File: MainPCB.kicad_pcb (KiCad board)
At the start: 2 copper layers, 1.7 x 9.8 mm, 78 parts, among them IC1 VNH7070ASTR, IC2 VNH7070ASTR, IC3 VNH7070ASTR, IC4 VNH7070ASTR, IC5 VNH7070ASTR, J1 Conn_01x06, J10 Conn_01x02, J11 Conn_01x03, J13 Conn_01x03, J14 Conn_01x02, J2 RaspberryPi, J4 Conn_01x02, J5 Screw_Terminal_01x02, J6 Conn_02x05_Odd_Even, J8 Conn_01x02, J9 Conn_01x02, M1 Motor_DC, M2 Motor_DC, M3 Motor_DC, M4 Motor_DC, M5 Motor_DC, SW1 SW_DPST_x2, SW2 SW_SPDT, SW3 SW_SPDT, SW4 SW_SPDT, SW5 SW_SPDT, SW6 SW_DPST_x2, U1 V_Regulator3.3v, U10 N channel, U12 Teensy4.1, U2 V_Regulator5v, U6 N channel

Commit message: Placement Done
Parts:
- removed C15: 0.1uf, Capacitor_SMD:C_0805_2012Metric_Pad1.18x1.45mm_HandSolder
- removed IC5: VNH7070ASTR, VNH:SOIC127P600X175-16N
- removed J13: Conn_01x03, Connector_PinHeader_2.54mm:PinHeader_1x03_P2.54mm_Vertical
- removed J14: Conn_01x02, Connector_JST:JST_XH_B2B-XH-A_1x02_P2.50mm_Vertical
- removed M5: Motor_DC, Connector_JST:JST_XH_B2B-XH-AM_1x02_P2.50mm_Vertical
- removed R19: 0, Resistor_SMD:R_0805_2012Metric_Pad1.20x1.40mm_HandSolder
- removed R20: 1, Resistor_SMD:R_0805_2012Metric_Pad1.20x1.40mm_HandSolder
- removed R23, R24, R25: 100, Resistor_SMD:R_0805_2012Metric_Pad1.20x1.40mm_HandSolder
- added J12: Conn_01x03, Connector_JST:JST_XH_B3B-XH-A_1x03_P2.50mm_Vertical, F.Cu at (143.5, 82.0)
- added J3: Conn_01x12, Connector_IDC:IDC-Header_2x06_P2.54mm_Vertical, B.Cu at (149.9, 92.9)
- added J7: Conn_01x02, Connector_JST:JST_XH_B2B-XH-A_1x02_P2.50mm_Vertical, F.Cu at (91.7, 69.3)
- added JP1: SolderJumper_2_Open, Jumper:SolderJumper-2_P1.3mm_Open_RoundedPad1.0x1.5mm, F.Cu at (91.5, 97.0)
- added JP2: SolderJumper_2_Open, Jumper:SolderJumper-2_P1.3mm_Open_RoundedPad1.0x1.5mm, F.Cu at (91.5, 100.5)
- added MOD1: RCJ-COM-2024, RCJ-COM-MOD:RCJ-COM-2024, F.Cu at (133.6, 147.8)
- added U3: BoostConverter, BoostConverter:Boost_Convertor_LM2577, F.Cu at (76.4, 141.2)
- added U4: BNO055, BNO055:BNO055, F.Cu at (119.0, 90.0)
- C11, C12, C13, C14, C3, C4, C5, C6, C7, C8, IC1, IC2, IC3, IC4, R1, R10, R11, R12, R13, R14, R15, R16, R17, R18, R2, R3, R4, R5, R6, R7, R9: moved to B.Cu
- J10, J8, J9: footprint Connector_PinHeader_2.54mm:PinHeader_1x02_P2.54mm_Vertical -> Connector_JST:JST_XH_B2B-XH-A_1x02_P2.50mm_Vertical
- J11: footprint Connector_PinHeader_2.54mm:PinHeader_1x03_P2.54mm_Vertical -> Connector_JST:JST_XH_B3B-XH-A_1x03_P2.50mm_Vertical; moved to B.Cu
- J6: value Conn_02x05_Odd_Even -> Conn_01x03; footprint Connector_IDC:IDC-Header_2x05_P2.54mm_Vertical -> Connector_JST:JST_XH_B3B-XH-A_1x03_P2.50mm_Vertical
- M1, M2, M3, M4: footprint Connector_JST:JST_XH_B2B-XH-AM_1x02_P2.50mm_Vertical -> Connector_JST:JST_XH_B2B-XH-A_1x02_P2.50mm_Vertical
- moved SW6 126.6 mm to (56.7, 126.7), turned to 90 degrees
- moved SW5 123.9 mm to (49.3, 80.1), turned to 90 degrees
- moved SW4 117.5 mm to (49.3, 86.1), turned to 90 degrees
- moved U12 114.1 mm to (76.7, 98.6)
- moved SW3 112.8 mm to (49.5, 111.8), turned to 90 degrees
- moved SW2 101.6 mm to (49.5, 117.8), turned to 90 degrees
- moved J6 100.9 mm to (107.0, 145.0), turned to -90 degrees
- moved IC3 100.2 mm to (84.6, 118.5)
- moved R5 98.8 mm to (58.2, 117.9), turned to 90 degrees
- moved R18 95.5 mm to (66.5, 126.8), turned to -90 degrees
- moved SW1 93.5 mm to (49.6, 71.8), turned to 90 degrees
- moved R6 92.5 mm to (58.1, 111.8), turned to 90 degrees
- moved C13 90.6 mm to (66.4, 118.2), turned to -90 degrees
- moved C10 82.3 mm to (48.9, 98.5)
- moved C9 82.3 mm to (48.9, 95.5)
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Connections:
- J6 pad 1: CS1 -> 48V
- J6 pad 2: SCK1 -> GND
- J6 pad 3: CS2 -> 12V
- U12 pad 19: unconnected-(U12-27_A13_SCK1-Pad19) -> CommModuleRun
- U12 pad 25: TRIG1 -> unconnected-(U12-33_MCLK2-Pad25)
- U12 pad 26: ECHO -> SLIDE2
- U12 pad 27: TRIG2 -> CS6
- U12 pad 28: SLIDE2 -> CS5
- U12 pad 29: TRIG3 -> CS4
- U12 pad 31: TRIG4 -> unconnected-(U12-39_MISO1_OUT1A-Pad31)
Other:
- board size 1.7 x 9.8 mm -> 126 x 89.5 mm
- board text added: "3.3V Reg"
- board text added: "5V Reg"
- board text added: "Robot 1"
- board text added: "Robot 2"

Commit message: PCB Done
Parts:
- R8: moved to B.Cu
- moved M1 37.7 mm to (98.9, 69.0)
- moved C11 34.7 mm to (102.5, 76.7)
- moved J4 22.0 mm to (164.8, 108.5), turned to 90 degrees
- moved C3 20.6 mm to (137.0, 100.3), turned to 90 degrees
- moved C4 16.9 mm to (139.8, 100.3), turned to 90 degrees
- moved C8 13.3 mm to (120.7, 100.4)
- moved C7 8.71 mm to (123.4, 100.4)
- moved R8 7.56 mm to (77.9, 85.3)
- moved U4 5.03 mm to (119.0, 95.1)
- moved J7 3.76 mm to (87.9, 69.2)
- moved R7 3.28 mm to (92.5, 79.4)
- moved C1 3.12 mm to (163.6, 101.7)
- moved C2 3.05 mm to (166.4, 101.6)
- moved M2 2.07 mm to (108.3, 68.8)
- moved C14 1.80 mm to (127.2, 119.3)
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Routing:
- net GND: track 0.00 -> 571.1 mm, vias 0 -> 4
- net 12V: track 0.00 -> 447.6 mm, vias 0 -> 36
- net 3.3V: track 0.00 -> 258.8 mm, vias 0 -> 1
- net 5V: track 0.00 -> 257.4 mm, vias 0 -> 6
- net Net-(J5-Pin_2): track 0.00 -> 143.5 mm, vias 0 -> 1
- net Net-(SW1A-B): track 0.00 -> 135.7 mm, vias 0 -> 1
- net STATE: track 0.00 -> 119.2 mm, vias 0 -> 1
- net TX2->RX: track 0.00 -> 116.3 mm, vias 0 -> 1
- net RX2->TX: track 0.00 -> 109.9 mm, vias 0 -> 1
- net PWM5: track 0.00 -> 99.6 mm, vias 0 -> 1
- net CS1: track 0.00 -> 90.3 mm, vias 0 -> 2
- net CommModuleRun: track 0.00 -> 86.3 mm, vias 0 -> 1
- net CS3: track 0.00 -> 86.2 mm, vias 0 -> 2
- net MOSI: track 0.00 -> 81.0 mm
- net RX7 -> TX: track 0.00 -> 78.5 mm
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- added copper zone on B.Cu, net GND
- added copper zone on F.Cu, net GND
- added copper zone on In1.Cu, net GND
- added copper zone on In2.Cu, net GND
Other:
- copper layers 2 -> 4

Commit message: Placed Everything for new version
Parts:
- removed J12, J6: Conn_01x03, Connector_JST:JST_XH_B3B-XH-A_1x03_P2.50mm_Vertical
- removed J7: Conn_01x02, Connector_JST:JST_XH_B2B-XH-A_1x02_P2.50mm_Vertical
- removed R6: 10k, Capacitor_SMD:C_0805_2012Metric_Pad1.18x1.45mm_HandSolder
- removed SW2, SW3, SW4, SW5: SW_SPDT, SlideSW:SPDT_OS102011_CNK
- removed U1: V_Regulator3.3v, Custom:Pololu5V3.4A
- removed U2: V_Regulator5v, Custom:Pololu5V3.4A
- added C15: 0.1uf, Capacitor_SMD:C_0805_2012Metric_Pad1.18x1.45mm_HandSolder, B.Cu at (131.3, 70.7)
- added C401: 100n, Capacitor_SMD:C_0402_1005Metric, B.Cu at (68.2, 86.2)
- added C501: 100n, Capacitor_SMD:C_0402_1005Metric, B.Cu at (106.0, 68.1)
- added C502: 100n, Capacitor_SMD:C_0402_1005Metric, B.Cu at (109.4, 70.8)
- added C601: 4u7, Capacitor_SMD:C_0805_2012Metric, F.Cu at (134.4, 122.8)
- added C602: 100n, Capacitor_SMD:C_0402_1005Metric, F.Cu at (134.4, 125.5)
- added C701: 10u, Capacitor_SMD:C_0805_2012Metric, F.Cu at (144.3, 75.8)
- added C702: 100uF, Capacitor_Tantalum_SMD:CP_EIA-7343-31_Kemet-D, B.Cu at (142.1, 80.3)
- added C703: 10u, Capacitor_SMD:C_0805_2012Metric, B.Cu at (142.7, 68.2)
- added D101: RCLAMP0502BA, Package_TO_SOT_SMD:SOT-416, F.Cu at (150.8, 68.3)
- added D401: PUSB3F96X, IP4292CZ10:DFN2510A-10_SOT1176-1_NEX, F.Cu at (106.0, 77.4)
- added D402: PUSB3F96X, IP4292CZ10:DFN2510A-10_SOT1176-1_NEX, F.Cu at (100.3, 77.2)
- added D403: PUSB3F96X, IP4292CZ10:DFN2510A-10_SOT1176-1_NEX, F.Cu at (111.4, 77.4)
- added D605: GREEN, Diode_SMD:D_0201_0603Metric_Pad0.64x0.40mm_HandSolder, F.Cu at (124.4, 66.4)
- added D606: GREEN, Diode_SMD:D_0201_0603Metric_Pad0.64x0.40mm_HandSolder, F.Cu at (95.6, 66.2)
- added D701: RCLAMP0502BA, Package_TO_SOT_SMD:SOT-416, F.Cu at (148.2, 66.8)
- added IC5: VNH7070ASTR, VNH:SOIC127P600X175-16N, B.Cu at (142.0, 96.6)
- added J101: TYPEC-305-ACP16H458, Connector_USB:USB_C_Receptacle_G-Switch_GT-USB-7010ASV, F.Cu at (151.4, 75.2)
- added J20: Conn_01x02_Pin, Connector_PinHeader_2.54mm:PinHeader_1x02_P2.54mm_Vertical, F.Cu at (148.5, 122.9)
- added J501: GT-HD001B-CNNG1, CM5IO:EDAC 690-019-298-412, F.Cu at (106.0, 73.5)
- added J802: Conn_01x22_Female, CM5IO:Hirose_FH12-22S-0.5SH_1x22-1MP_P0.50mm_Horizontal, F.Cu at (105.8, 144.3)
- added M5: Motor_DC, Connector_JST:JST_XH_B2B-XH-A_1x02_P2.50mm_Vertical, F.Cu at (129.9, 68.2)
- added Module1: ComputeModule5-CM5, CM5IO:Raspberry-Pi-5-Compute-Module, F.Cu at (150.0, 117.4)
- added R104: 10k, Resistor_SMD:R_0402_1005Metric, B.Cu at (123.7, 113.1)
- added R401: 470R, Resistor_SMD:R_0402_1005Metric, B.Cu at (65.0, 89.0)
- added R402: 470R, Resistor_SMD:R_0402_1005Metric, B.Cu at (65.6, 86.8)
- added R605: 2k2, Resistor_SMD:R_0402_1005Metric, F.Cu at (123.6, 67.8)
- added R606: 2k2, Resistor_SMD:R_0402_1005Metric, F.Cu at (95.1, 69.6)
- added R701: 15k, Resistor_SMD:R_0402_1005Metric, F.Cu at (143.4, 73.5)
- added R702: 22k, Resistor_SMD:R_0402_1005Metric, B.Cu at (139.4, 68.8)
- added R703: 22k, Resistor_SMD:R_0402_1005Metric, B.Cu at (139.3, 67.1)
- added S1: TS04-66-70-BK-100-SMT, TS04:SW_TS04-66-70-BK-100-SMT, F.Cu at (132.5, 148.4)
- added T401: 7498111120AR, Ethernet:7498111120AR, F.Cu at (58.5, 79.4)
- added U401: TPD4EUSB30, Package_SON:USON-10_2.5x1.0mm_P0.5mm, F.Cu at (57.5, 86.7)
- added U402: TPD4EUSB30, Package_SON:USON-10_2.5x1.0mm_P0.5mm, F.Cu at (60.9, 86.7)
- added U405: STMPS2151STR, Package_TO_SOT_SMD:SOT-23-5, B.Cu at (109.2, 68.0)
- added U602: SN74LVC1G14DBVR, Package_TO_SOT_SMD:SOT-353_SC-70-5, B.Cu at (124.6, 71.0)
- added U701: AP22653W6, Package_TO_SOT_SMD:SOT-23-6, B.Cu at (143.9, 74.7)
- added USB701: TYPEC-305-ACP16H458, Connector_USB:USB_C_Receptacle_G-Switch_GT-USB-7010ASV, F.Cu at (141.2, 67.8)
- C10, C9: moved to B.Cu
- C5, C6, J11: moved to F.Cu
- J2: value RaspberryPi -> Conn_01x05_Pin; footprint Connector_JST:JST_XH_B4B-XH-AM_1x04_P2.50mm_Vertical -> Connector_JST:JST_XH_B5B-XH-A_1x05_P2.50mm_Vertical
- J5: footprint Connector_AMASS:AMASS_XT60PW-F_1x02_P7.20mm_Horizontal -> Connector_AMASS:AMASS_XT60-F_1x02_P7.20mm_Vertical
- R3, R4, R5: value 10k -> 100; footprint Capacitor_SMD:C_0805_2012Metric_Pad1.18x1.45mm_HandSolder -> Resistor_SMD:R_0805_2012Metric_Pad1.20x1.40mm_HandSolder
- moved J1 124.5 mm to (46.9, 76.8)
- moved J4 117.6 mm to (47.4, 116.3)
- moved J3 117.3 mm to (32.6, 90.7), turned to 180 degrees
- moved C2 115.8 mm to (51.4, 88.2)
- moved C1 109.8 mm to (54.6, 88.1)
- moved C4 101.5 mm to (38.3, 101.9)
- moved J11 96.5 mm to (143.6, 124.9), turned to -90 degrees
- moved C3 96.0 mm to (41.0, 101.9)
- moved J5 90.0 mm to (55.6, 123.4), turned to 90 degrees
- moved U10 89.7 mm to (65.2, 119.7), turned to 90 degrees
- moved R4 86.9 mm to (143.9, 103.9), turned to 0 degrees
- moved R3 84.5 mm to (143.3, 88.6), turned to 0 degrees
- moved R5 82.4 mm to (139.6, 104.5), turned to -90 degrees
- moved H4 75.9 mm to (129.0, 75.5)
- moved H6 75.9 mm to (71.0, 75.5)
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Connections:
- net SLIDE2 renamed DIR5A
- J2 pad 1: 5V -> 12V
- J2 pad 2: GND -> 5V
- J2 pad 3: RX2->TX -> 3.3V
- J2 pad 4: TX2->RX -> GND
- R3 pad 2: GND -> Net-(IC5-IN_A)
- R4 pad 1: SLIDE4 -> DIR5B
- R4 pad 2: GND -> Net-(IC5-IN_B)
- R5 pad 1: SLIDE1 -> Net-(IC5-PWM)
- R5 pad 2: GND -> PWM5
- U12 pad 10: TX2->RX -> CS2
- U12 pad 23: SLIDE1 -> DIR3B
- U12 pad 24: unconnected-(U12-32_OUT1B-Pad24) -> UART3_RTS -> CTS
- U12 pad 25: unconnected-(U12-33_MCLK2-Pad25) -> DIR5B
- U12 pad 30: SLIDE3 -> unconnected-(U12-38_CS1_IN1-Pad30)
- U12 pad 32: SLIDE4 -> unconnected-(U12-40_A16-Pad32)
- U12 pad 36: CS1 -> TX3->RX
- U12 pad 37: CS2 -> RX3->TX
- U12 pad 41: DIR3B -> UART3_CTS -> RTS
- U12 pad 9: RX2->TX -> CS1
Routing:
- net GND: track 571.1 -> 0.00 mm, vias 4 -> 0
- net 12V: track 447.6 -> 114.1 mm, vias 36 -> 15
- net 3.3V: track 258.8 -> 0.00 mm, vias 1 -> 0
- net 5V: track 257.4 -> 0.00 mm, vias 6 -> 0
- net Net-(SW1A-B): track 135.7 -> 0.00 mm, vias 1 -> 0
- net Net-(J5-Pin_2): track 143.5 -> 11.3 mm, vias 1 -> 0
- net STATE: track 119.2 -> 0.00 mm, vias 1 -> 0
- net TX2->RX: track 116.3 -> 0.00 mm, vias 1 -> 0
- net RX2->TX: track 109.9 -> 0.00 mm, vias 1 -> 0
- net PWM5: track 99.6 -> 0.00 mm, vias 1 -> 0
- net CS1: track 90.3 -> 0.00 mm, vias 2 -> 0
- net CommModuleRun: track 86.3 -> 0.00 mm, vias 1 -> 0
- net CS3: track 86.2 -> 0.00 mm, vias 2 -> 0
- net MOSI: track 81.0 -> 0.00 mm
- net RX7 -> TX: track 78.5 -> 0.00 mm
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- removed copper zone on B.Cu, net GND
- removed copper zone on F.Cu, net GND
- removed copper zone on In1.Cu, net GND
- removed copper zone on In2.Cu, net GND
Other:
- board size 126 x 89.5 mm -> 128 x 89.5 mm
- board text removed: "3.3V Reg"
- board text removed: "5V Reg"

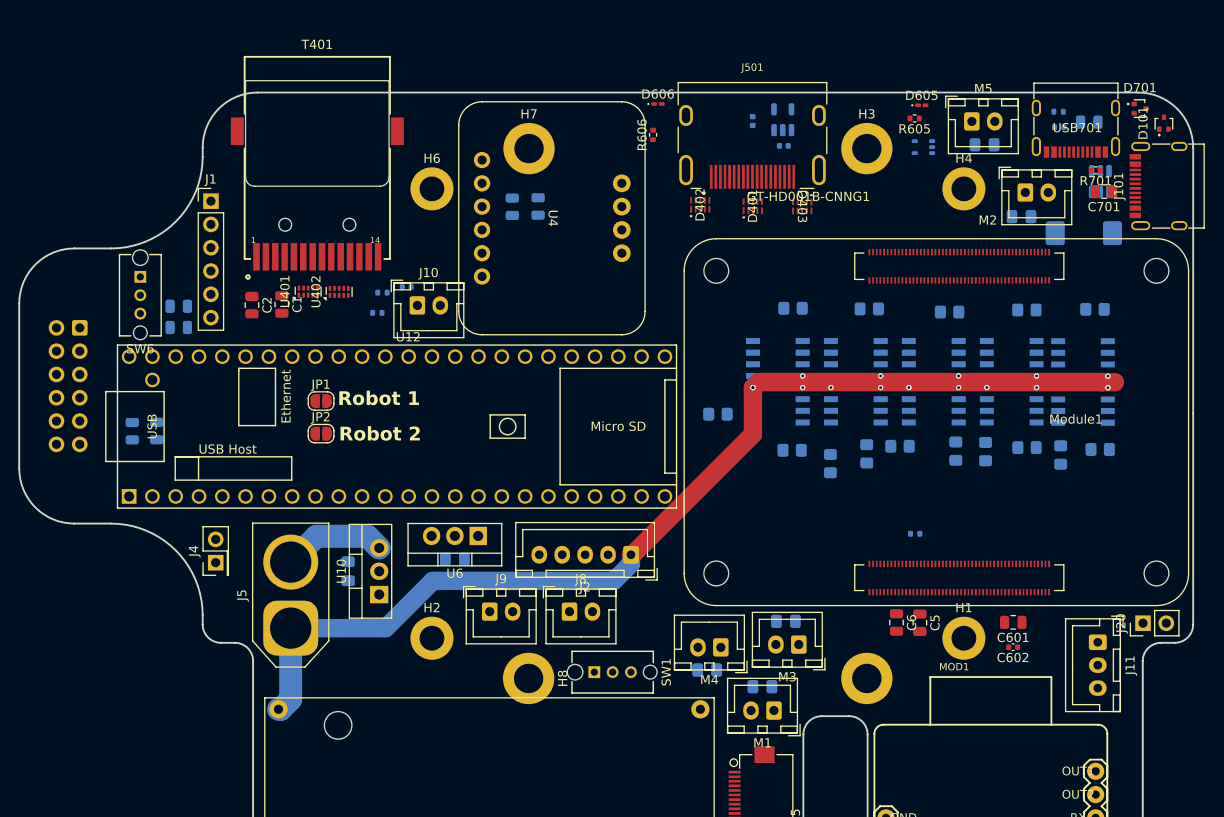
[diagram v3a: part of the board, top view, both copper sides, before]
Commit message: Finished Power Wiring and Fixed Schematic Bus Issues
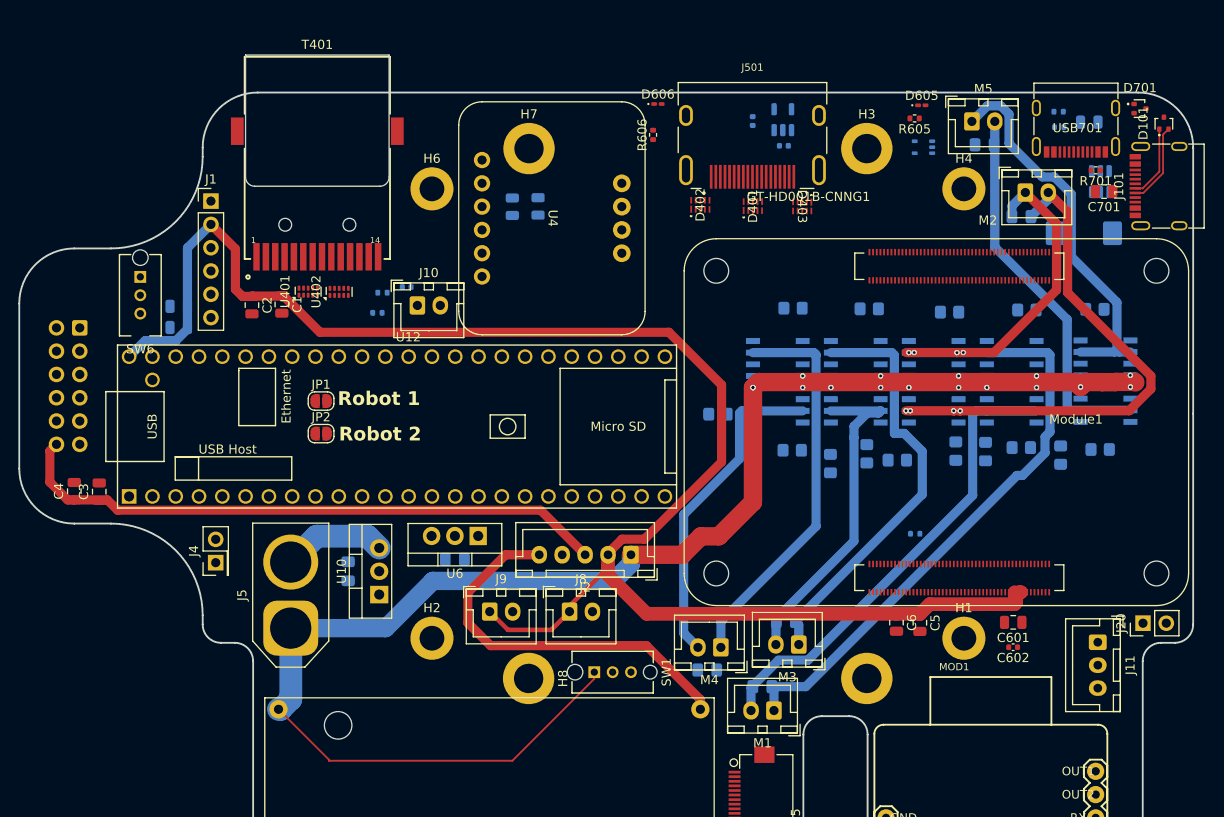
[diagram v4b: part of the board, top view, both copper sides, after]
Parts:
- C3, C4: moved to F.Cu
- moved C3 9.10 mm to (34.7, 108.5)
- moved C4 9.09 mm to (32.0, 108.5)
- moved IC5 2.45 mm to (144.4, 96.5)
- moved R11 1.54 mm to (121.7, 105.1)
- moved R7 0.63 mm to (135.3, 103.7)
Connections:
- D401 pad 1: /HDMI/HDMI_C.D0_P -> /CM5/HDMI_PI.D0_P
- D401 pad 10: /HDMI/HDMI_C.D0_P -> /CM5/HDMI_PI.D0_P
- D401 pad 2: /HDMI/HDMI_C.D0_N -> /CM5/HDMI_PI.D0_N
- D401 pad 4: /HDMI/HDMI_C.CK_P -> /CM5/HDMI_PI.CK_P
- D401 pad 5: /HDMI/HDMI_C.CK_N -> /CM5/HDMI_PI.CK_N
- D401 pad 6: /HDMI/HDMI_C.CK_N -> /CM5/HDMI_PI.CK_N
- D401 pad 7: /HDMI/HDMI_C.CK_P -> /CM5/HDMI_PI.CK_P
- D401 pad 9: /HDMI/HDMI_C.D0_N -> /CM5/HDMI_PI.D0_N
- D402 pad 1: /HDMI/HDMI_C.D2_P -> /CM5/HDMI_PI.D2_P
- D402 pad 10: /HDMI/HDMI_C.D2_P -> /CM5/HDMI_PI.D2_P
- D402 pad 2: /HDMI/HDMI_C.D2_N -> /CM5/HDMI_PI.D2_N
- D402 pad 4: /HDMI/HDMI_C.D1_P -> /CM5/HDMI_PI.D1_P
- D402 pad 5: /HDMI/HDMI_C.D1_N -> /CM5/HDMI_PI.D1_N
- D402 pad 6: /HDMI/HDMI_C.D1_N -> /CM5/HDMI_PI.D1_N
- D402 pad 7: /HDMI/HDMI_C.D1_P -> /CM5/HDMI_PI.D1_P
- D402 pad 9: /HDMI/HDMI_C.D2_N -> /CM5/HDMI_PI.D2_N
- D403 pad 1: /HDMI/HDMI_C.CEC -> /CM5/HDMI_PI.CEC
- D403 pad 10: /HDMI/HDMI_C.CEC -> /CM5/HDMI_PI.CEC
- D403 pad 2: /HDMI/HDMI_C.HOTPLUG -> /CM5/HDMI_PI.HOTPLUG
- D403 pad 4: /HDMI/HDMI_C.SDA -> /CM5/HDMI_PI.SDA
- D403 pad 5: /HDMI/HDMI_C.SCL -> /CM5/HDMI_PI.SCL
- D403 pad 6: /HDMI/HDMI_C.SCL -> /CM5/HDMI_PI.SCL
- D403 pad 7: /HDMI/HDMI_C.SDA -> /CM5/HDMI_PI.SDA
- D403 pad 9: /HDMI/HDMI_C.HOTPLUG -> /CM5/HDMI_PI.HOTPLUG
- D701 pad 1: /USB/USB2C.D_P -> /CM5/USB2P.D_P
- D701 pad 2: /USB/USB2C.D_N -> /CM5/USB2P.D_N
- J501 pad 1: /HDMI/HDMI_C.D2_P -> /CM5/HDMI_PI.D2_P
- J501 pad 10: /HDMI/HDMI_C.CK_P -> /CM5/HDMI_PI.CK_P
- J501 pad 12: /HDMI/HDMI_C.CK_N -> /CM5/HDMI_PI.CK_N
- J501 pad 13: /HDMI/HDMI_C.CEC -> /CM5/HDMI_PI.CEC
- J501 pad 15: /HDMI/HDMI_C.SCL -> /CM5/HDMI_PI.SCL
- J501 pad 16: /HDMI/HDMI_C.SDA -> /CM5/HDMI_PI.SDA
- J501 pad 19: /HDMI/HDMI_C.HOTPLUG -> /CM5/HDMI_PI.HOTPLUG
- J501 pad 3: /HDMI/HDMI_C.D2_N -> /CM5/HDMI_PI.D2_N
- J501 pad 4: /HDMI/HDMI_C.D1_P -> /CM5/HDMI_PI.D1_P
- J501 pad 6: /HDMI/HDMI_C.D1_N -> /CM5/HDMI_PI.D1_N
- J501 pad 7: /HDMI/HDMI_C.D0_P -> /CM5/HDMI_PI.D0_P
- J501 pad 9: /HDMI/HDMI_C.D0_N -> /CM5/HDMI_PI.D0_N
- J802 pad 11: /DSI_CSI/DPHY0_C.D2_N -> /CM5/DPHY0_P.D2_N
- J802 pad 12: /DSI_CSI/DPHY0_C.D2_P -> /CM5/DPHY0_P.D2_P
- J802 pad 14: /DSI_CSI/DPHY0_C.D3_N -> /CM5/DPHY0_P.D3_N
- J802 pad 15: /DSI_CSI/DPHY0_C.D3_P -> /CM5/DPHY0_P.D3_P
- J802 pad 2: /DSI_CSI/DPHY0_C.D0_N -> /CM5/DPHY0_P.D0_N
- J802 pad 3: /DSI_CSI/DPHY0_C.D0_P -> /CM5/DPHY0_P.D0_P
- J802 pad 5: /DSI_CSI/DPHY0_C.D1_N -> /CM5/DPHY0_P.D1_N
- J802 pad 6: /DSI_CSI/DPHY0_C.D1_P -> /CM5/DPHY0_P.D1_P
- J802 pad 8: /DSI_CSI/DPHY0_C.C_N -> /CM5/DPHY0_P.C_N
- J802 pad 9: /DSI_CSI/DPHY0_C.C_P -> /CM5/DPHY0_P.C_P
- Module1 pad 103: /CM5/USB_PI.D_N -> /USB_C.D_N
- Module1 pad 105: /CM5/USB_PI.D_P -> /USB_C.D_P
- R3 pad 1: DIR5A -> DIR4A
- R4 pad 1: DIR5B -> DIR4B
- R5 pad 2: PWM5 -> PWM4
- T401 pad 10: /Ethernet/ETH_C.TRD3_N -> /CM5/ETH_PI.TRD3_N
- T401 pad 3: /Ethernet/ETH_C.TRD0_P -> /CM5/ETH_PI.TRD0_P
- T401 pad 4: /Ethernet/ETH_C.TRD0_N -> /CM5/ETH_PI.TRD0_N
- T401 pad 5: /Ethernet/ETH_C.TRD1_P -> /CM5/ETH_PI.TRD1_P
- T401 pad 6: /Ethernet/ETH_C.TRD1_N -> /CM5/ETH_PI.TRD1_N
- T401 pad 7: /Ethernet/ETH_C.TRD2_P -> /CM5/ETH_PI.TRD2_P
- T401 pad 8: /Ethernet/ETH_C.TRD2_N -> /CM5/ETH_PI.TRD2_N
- T401 pad 9: /Ethernet/ETH_C.TRD3_P -> /CM5/ETH_PI.TRD3_P
- U12 pad 25: DIR5B -> unconnected-(U12-33_MCLK2-Pad25)
- U12 pad 26: DIR5A -> unconnected-(U12-34_RX8-Pad26)
- U401 pad 1: /Ethernet/ETH_C.TRD0_P -> /CM5/ETH_PI.TRD0_P
- U401 pad 10: /Ethernet/ETH_C.TRD0_P -> /CM5/ETH_PI.TRD0_P
- U401 pad 2: /Ethernet/ETH_C.TRD0_N -> /CM5/ETH_PI.TRD0_N
- U401 pad 4: /Ethernet/ETH_C.TRD1_P -> /CM5/ETH_PI.TRD1_P
- U401 pad 5: /Ethernet/ETH_C.TRD1_N -> /CM5/ETH_PI.TRD1_N
- U401 pad 6: /Ethernet/ETH_C.TRD1_N -> /CM5/ETH_PI.TRD1_N
- U401 pad 7: /Ethernet/ETH_C.TRD1_P -> /CM5/ETH_PI.TRD1_P
- U401 pad 9: /Ethernet/ETH_C.TRD0_N -> /CM5/ETH_PI.TRD0_N
- U402 pad 1: /Ethernet/ETH_C.TRD2_P -> /CM5/ETH_PI.TRD2_P
- U402 pad 10: /Ethernet/ETH_C.TRD2_P -> /CM5/ETH_PI.TRD2_P
- U402 pad 2: /Ethernet/ETH_C.TRD2_N -> /CM5/ETH_PI.TRD2_N
- U402 pad 4: /Ethernet/ETH_C.TRD3_P -> /CM5/ETH_PI.TRD3_P
- U402 pad 5: /Ethernet/ETH_C.TRD3_N -> /CM5/ETH_PI.TRD3_N
- U402 pad 6: /Ethernet/ETH_C.TRD3_N -> /CM5/ETH_PI.TRD3_N
- U402 pad 7: /Ethernet/ETH_C.TRD3_P -> /CM5/ETH_PI.TRD3_P
- U402 pad 9: /Ethernet/ETH_C.TRD2_N -> /CM5/ETH_PI.TRD2_N
- USB701 pad A6: /USB/USB2C.D_P -> /CM5/USB2P.D_P
- USB701 pad A7: /USB/USB2C.D_N -> /CM5/USB2P.D_N
- USB701 pad B6: /USB/USB2C.D_P -> /CM5/USB2P.D_P
- USB701 pad B7: /USB/USB2C.D_N -> /CM5/USB2P.D_N
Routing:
- net 5V: track 0.00 -> 178.8 mm
- net 3.3V: track 0.00 -> 66.1 mm
- net Net-(IC1-OUT_A_1): track 0.00 -> 60.9 mm
- net Net-(IC2-OUT_B_1): track 0.00 -> 57.2 mm, vias 0 -> 4
- net Net-(IC1-OUT_B_1): track 0.00 -> 51.3 mm
- net 12V: track 114.1 -> 162.4 mm, vias 15 -> 16
- net Net-(IC3-OUT_A_1): track 0.00 -> 46.4 mm
- net Net-(IC4-OUT_A_1): track 0.00 -> 43.2 mm
- net 48V: track 0.00 -> 42.7 mm
- net Net-(IC5-OUT_A_1): track 0.00 -> 42.1 mm
- net Net-(IC5-OUT_B_1): track 0.00 -> 41.5 mm
- net Net-(IC3-OUT_B_1): track 0.00 -> 36.4 mm
- net Net-(IC4-OUT_B_1): track 0.00 -> 35.7 mm
- net Net-(IC2-OUT_A_1): track 0.00 -> 34.5 mm, vias 0 -> 4
- net /USB_C.D_N: track 0.00 -> 8.97 mm
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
